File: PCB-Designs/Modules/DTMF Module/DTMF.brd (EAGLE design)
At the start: 18 parts, among them IC1 CM8870CP

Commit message: change
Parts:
- removed CRY: 3.57, special:QS
- added OSC: 3.57, special:QS
- C1: value 0.47UF -> 0.47uf; device resistor:C050-024X044 -> capacitor-wima:C2.5-2
- C2, C3, C4: device resistor:C050-024X044 -> capacitor-wima:C2.5-2
- INPUT, POWER: device con-weidmueller-sl35:180-2 -> con-amp-quick:02P
- LED1, LED2, LED3, LED4: value (none) -> 3mm; device led:LED2X5 -> led:LED3MM
- OUTPUT1, OUTPUT2: device con-weidmueller-sl35:180-2 -> jumper:JP1
- R4: value 330 -> 330E
- moved OUTPUT1 47.4 mm to (61.0, 64.8), turned to 180 degrees
- moved C1 34.1 mm to (35.6, 54.6), turned to 270 degrees
- moved OUTPUT2 31.4 mm to (61.0, 54.6), turned to 180 degrees
- moved R2 29.8 mm to (34.3, 48.3)
- moved LED1 29.0 mm to (61.0, 45.7)
- moved R3 27.3 mm to (50.8, 63.5)
- moved INPUT 26.8 mm to (27.9, 61.0)
- moved POWER 25.6 mm to (27.9, 66.0)
- moved IC1 24.3 mm to (45.7, 43.2)
- moved C2 23.3 mm to (26.7, 38.1), turned to 180 degrees
- moved C3 23.3 mm to (26.7, 31.8), turned to 180 degrees
- moved R1 22.2 mm to (25.4, 53.3), turned to 180 degrees
- moved LED2 20.5 mm to (61.0, 40.6)
- moved C4 18.8 mm to (43.2, 66.0), turned to 90 degrees
- moved R4 17.7 mm to (48.3, 27.9), turned to 180 degrees
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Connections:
- net S$1 renamed N$12
- net S$8 renamed N$3
- removed net N$13 (its old number): C1.1, R1.1
- removed net N$17 (its old number): POWER.1
- removed net N$21: C2.1, C3.1, IC1.9, R4.1
- removed net N$22: IC1.5, IC1.6
- removed net N$23: IC1.14, LED4.A
- removed net N$24 (its old number): IC1.13, LED3.A
- removed net N$26: IC1.10, IC1.18
- removed net S$10: IC1.11
- removed net S$11: IC1.12, LED2.A
- removed net S$17: LED1.A
- removed net S$18: LED1.K, LED2.K, LED3.K, LED4.K, R4.2
- removed net S$2: C1.2
- removed net S$4: C2.2
- removed net S$5: C3.2, IC1.8
- new net N$1: C2.2, C3.2, IC1.5, IC1.6, IC1.9, INPUT.2, POWER.2, R4.2
- new net N$10: C4.1, IC1.10, IC1.18, POWER.1
- new net N$11: C1.1, INPUT.1
- new net N$14: C2.1, IC1.7, OSC.1
- new net N$15: C3.1, IC1.8, OSC.2
- new net N$2: C1.2, R1.1
- new net N$5: IC1.11, LED4.A, OUTPUT1.2
- new net N$6: IC1.12, LED3.A, OUTPUT1.1
- new net N$7: IC1.13, LED2.A, OUTPUT2.2
- new net N$8: IC1.14, LED1.A, OUTPUT2.1
- net N$4: now also LED1.K, LED2.K, LED3.K, LED4.K, R4.1; no longer POWER.2
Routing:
- net S$3: track 243.8 -> 0.00 mm
- net N$21: track 106.7 -> 0.00 mm
- net N$1: track 0.00 -> 89.5 mm
- net N$10: track 0.00 -> 83.4 mm
- net N$5: track 0.00 -> 80.1 mm
- net N$26: track 71.1 -> 0.00 mm
- net N$6: track 0.00 -> 56.2 mm
- net N$12: track 21.6 -> 63.9 mm
- net N$15: track 0.00 -> 31.4 mm
- net S$18: track 26.7 -> 0.00 mm
- net N$4: track 0.00 -> 26.5 mm
- net N$8: track 0.00 -> 26.5 mm
- net N$24 (its old number): track 24.1 -> 0.00 mm
- net N$23: track 24.1 -> 0.00 mm
- net N$7: track 0.00 -> 22.9 mm
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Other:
- board outline added: 100 x 80 mm
- board text removed: "WWW.COMPUTRONICSLAB.COM"

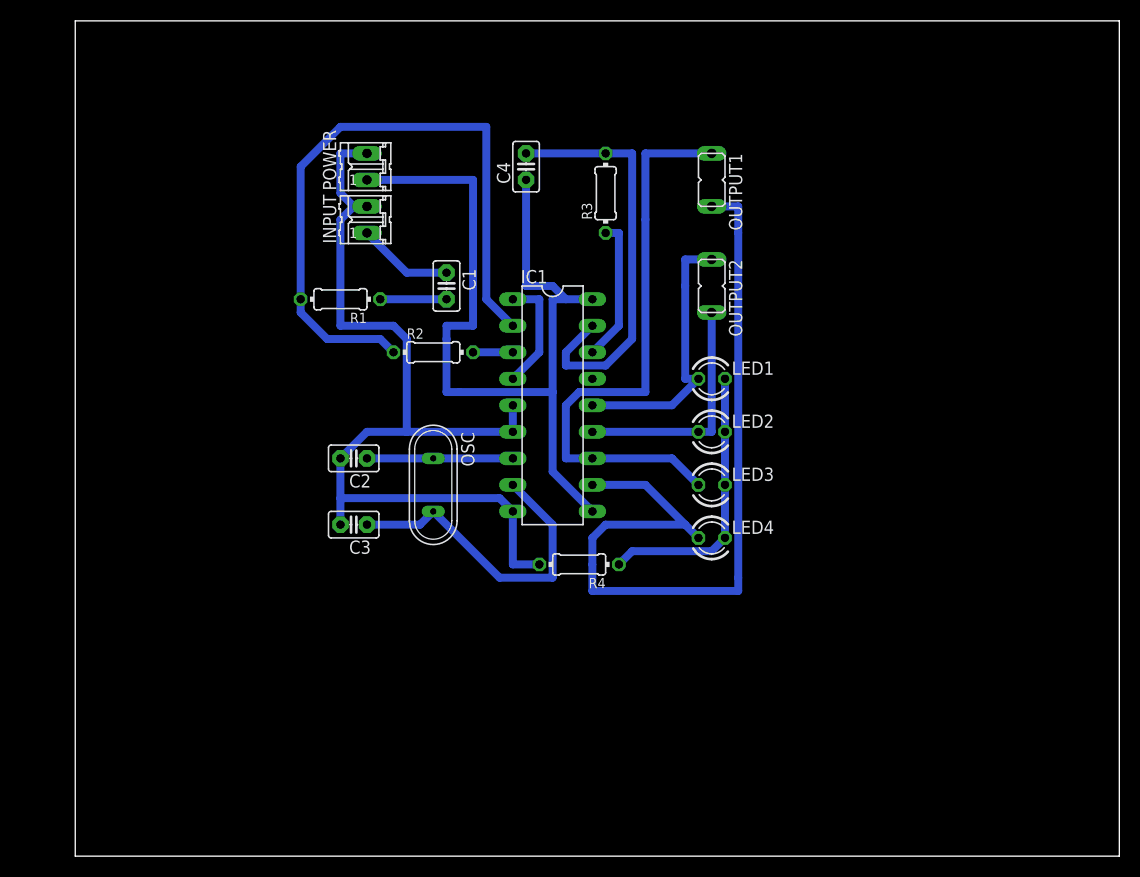
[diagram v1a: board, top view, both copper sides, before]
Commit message: 
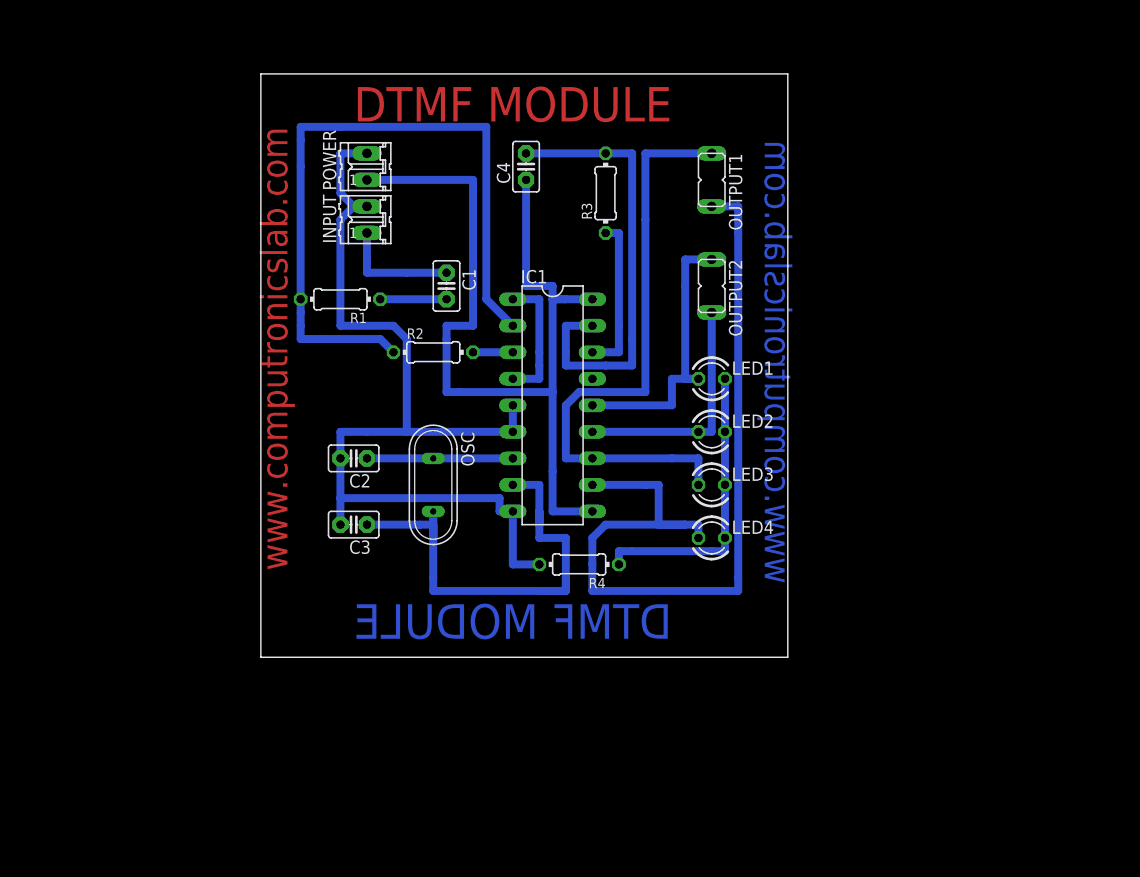
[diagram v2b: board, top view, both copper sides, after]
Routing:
- net N$15: track 31.4 -> 52.1 mm
- net N$12: track 63.9 -> 67.6 mm
- net N$5: track 80.1 -> 83.1 mm
- net N$10: track 83.4 -> 86.4 mm
- net N$24: track 40.2 -> 43.2 mm
- net N$1: track 89.5 -> 91.7 mm
- net N$11: track 9.20 -> 11.4 mm
- net N$13: track 11.2 -> 12.7 mm
- net N$8: track 26.5 -> 27.9 mm
- net N$6: track 56.2 -> 57.7 mm
- net N$4: track 26.5 -> 27.9 mm
- net N$17: track 13.8 -> 15.2 mm
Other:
- board size 100 x 80 mm -> 50.5 x 55.9 mm
- board text added: "DTMF MODULE"
- board text added: "www.computronicslab.com"
